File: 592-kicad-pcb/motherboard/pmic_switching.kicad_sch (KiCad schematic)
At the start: 10 parts

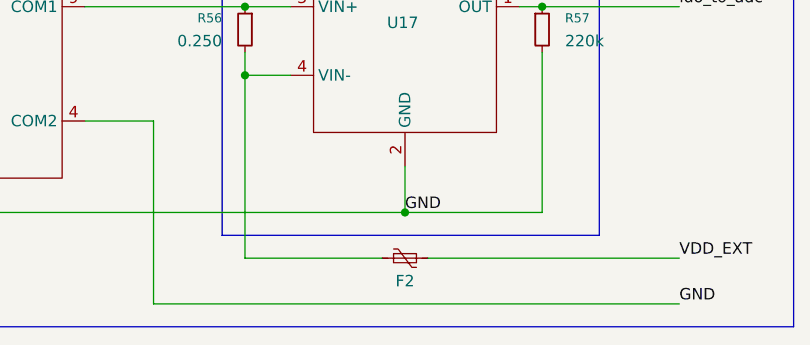
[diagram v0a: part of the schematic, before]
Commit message: fuse, fb info in values
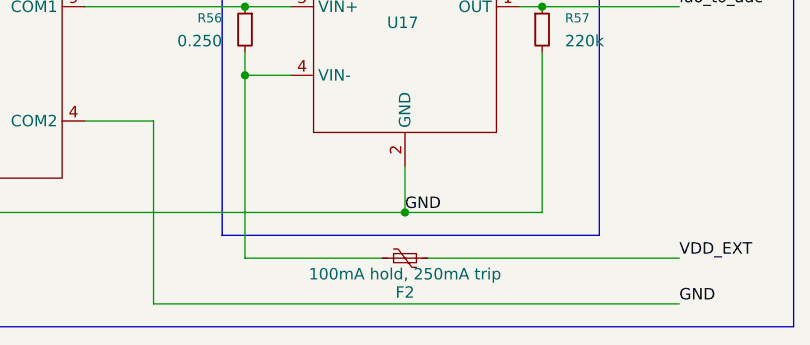
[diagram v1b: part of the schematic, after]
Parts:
- F2: value ~ -> 100mA hold, 250mA trip
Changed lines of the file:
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@@
 		(dnp no)
 		(property "Reference" "F2"
-			(at 137.16 160.02 90)
+			(at 137.16 161.29 90)
 			(effects
 				(font
@@
 			)
 		)
-		(property "Value" "~"
+		(property "Value" "100mA hold, 250mA trip"
 			(at 137.16 159.258 90)
 			(effects

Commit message: updates to routing
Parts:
- renumbered R54 to R60, R56 to R61, R55 to R62, R57 to R63, U20 to U24, U18 to U25, U19 to U26, U16 to U27, U17 to U28
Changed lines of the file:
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@@
 		(on_board yes)
 		(dnp no)
-		(property "Reference" "R57"
+		(property "Reference" "R63"
 			(at 154.94 130.8099 0)
 			(effects
@@
 			(project "motherboard"
 				(path "/5b0c97ac-fa03-4db8-b41b-0eee32b6f55d/f049e4ad-bebe-4338-850a-2727de737ae9/260af3dc-9286-4c76-9c6c-eeb806d3e6e5"
-					(reference "R57")
+					(reference "R63")
 					(unit 1)
 				)
@@
 		(on_board yes)
 		(dnp no)
-		(property "Reference" "U17"
+		(property "Reference" "U28"
 			(at 136.906 131.318 0)
 			(effects
@@
 			(project ""
 				(path "/5b0c97ac-fa03-4db8-b41b-0eee32b6f55d/f049e4ad-bebe-4338-850a-2727de737ae9/260af3dc-9286-4c76-9c6c-eeb806d3e6e5"
-					(reference "U17")
+					(reference "U28")
 					(unit 1)
 				)
@@
 		(on_board yes)
 		(dnp no)
-		(property "Reference" "U20"
+		(property "Reference" "U24"
 			(at 85.344 34.798 0)
 			(effects
@@
 			(project "motherboard"
 				(path "/5b0c97ac-fa03-4db8-b41b-0eee32b6f55d/f049e4ad-bebe-4338-850a-2727de737ae9/260af3dc-9286-4c76-9c6c-eeb806d3e6e5"
-					(reference "U20")
+					(reference "U24")
 					(unit 1)
 				)
@@
 		(on_board yes)
 		(dnp no)
-		(property "Reference" "U19"
+		(property "Reference" "U26"
 			(at 84.836 134.366 0)
 			(effects
@@
 			(project ""
 				(path "/5b0c97ac-fa03-4db8-b41b-0eee32b6f55d/f049e4ad-bebe-4338-850a-2727de737ae9/260af3dc-9286-4c76-9c6c-eeb806d3e6e5"
-					(reference "U19")
+					(reference "U26")
 					(unit 1)
 				)
@@
 		(on_board yes)
 		(dnp no)
-		(property "Reference" "U18"
+		(property "Reference" "U25"
 			(at 85.344 80.518 0)
 			(effects
@@
 			(project ""
 				(path "/5b0c97ac-fa03-4db8-b41b-0eee32b6f55d/f049e4ad-bebe-4338-850a-2727de737ae9/260af3dc-9286-4c76-9c6c-eeb806d3e6e5"
-					(reference "U18")
+					(reference "U25")
 					(unit 1)
 				)
@@
 		(on_board yes)
 		(dnp no)
-		(property "Reference" "U16"
+		(property "Reference" "U27"
 			(at 137.668 78.232 0)
 			(effects
@@
 			(project ""
 				(path "/5b0c97ac-fa03-4db8-b41b-0eee32b6f55d/f049e4ad-bebe-4338-850a-2727de737ae9/260af3dc-9286-4c76-9c6c-eeb806d3e6e5"
-					(reference "U16")
+					(reference "U27")
 					(unit 1)
 				)
@@
 		(on_board yes)
 		(dnp no)
-		(property "Reference" "R55"
+		(property "Reference" "R62"
 			(at 154.94 77.4699 0)
 			(effects
@@
 			(project "motherboard"
 				(path "/5b0c97ac-fa03-4db8-b41b-0eee32b6f55d/f049e4ad-bebe-4338-850a-2727de737ae9/260af3dc-9286-4c76-9c6c-eeb806d3e6e5"
-					(reference "R55")
+					(reference "R62")
 					(unit 1)
 				)
@@
 		(on_board yes)
 		(dnp no)
-		(property "Reference" "R56"
+		(property "Reference" "R61"
 			(at 116.84 130.8099 0)
 			(effects
@@
 			(project "motherboard"
 				(path "/5b0c97ac-fa03-4db8-b41b-0eee32b6f55d/f049e4ad-bebe-4338-850a-2727de737ae9/260af3dc-9286-4c76-9c6c-eeb806d3e6e5"
-					(reference "R56")
+					(reference "R61")
 					(unit 1)
 				)
@@
 		(on_board yes)
 		(dnp no)
-		(property "Reference" "R54"
+		(property "Reference" "R60"
 			(at 116.84 77.4699 0)
 			(effects
@@
 			(project ""
 				(path "/5b0c97ac-fa03-4db8-b41b-0eee32b6f55d/f049e4ad-bebe-4338-850a-2727de737ae9/260af3dc-9286-4c76-9c6c-eeb806d3e6e5"
-					(reference "R54")
-					(unit 1)
-				)
+					(reference "R60")
+					(unit 1)
+				)

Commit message: pins out progress
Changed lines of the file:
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@@
 		(exclude_from_sim no)
 		(at 116.84 63.5 0)
-		(size 41.91 38.1)
+		(size 43.18 38.1)
 		(margins 0.9525 0.9525 0.9525 0.9525)
 		(stroke
@@
 		(exclude_from_sim no)
 		(at 116.84 116.84 0)
-		(size 41.91 38.1)
+		(size 43.18 38.1)
 		(margins 0.9525 0.9525 0.9525 0.9525)
 		(stroke

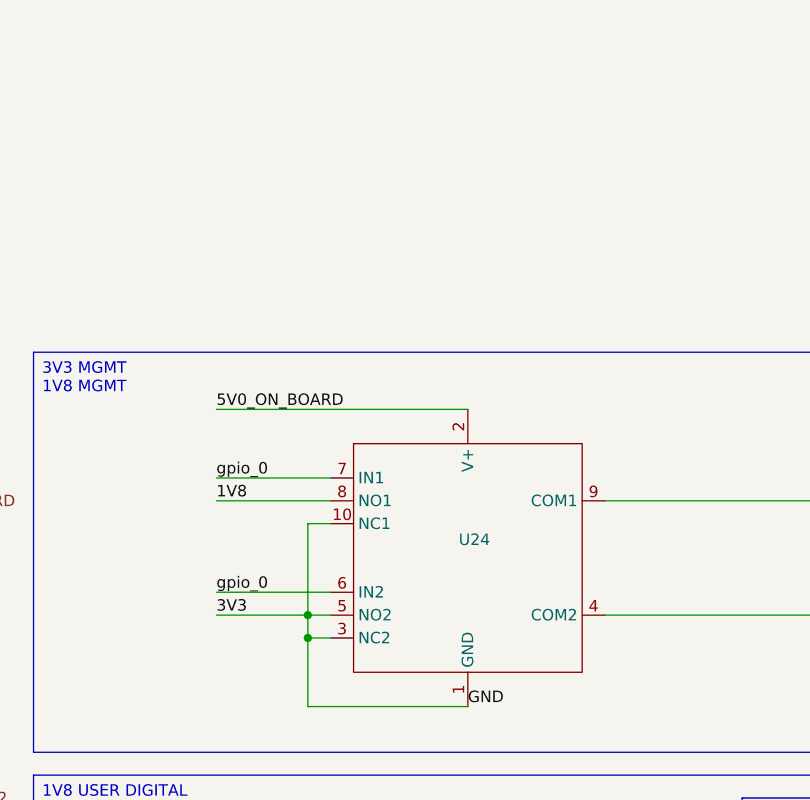
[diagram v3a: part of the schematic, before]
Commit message: can't work on one machine
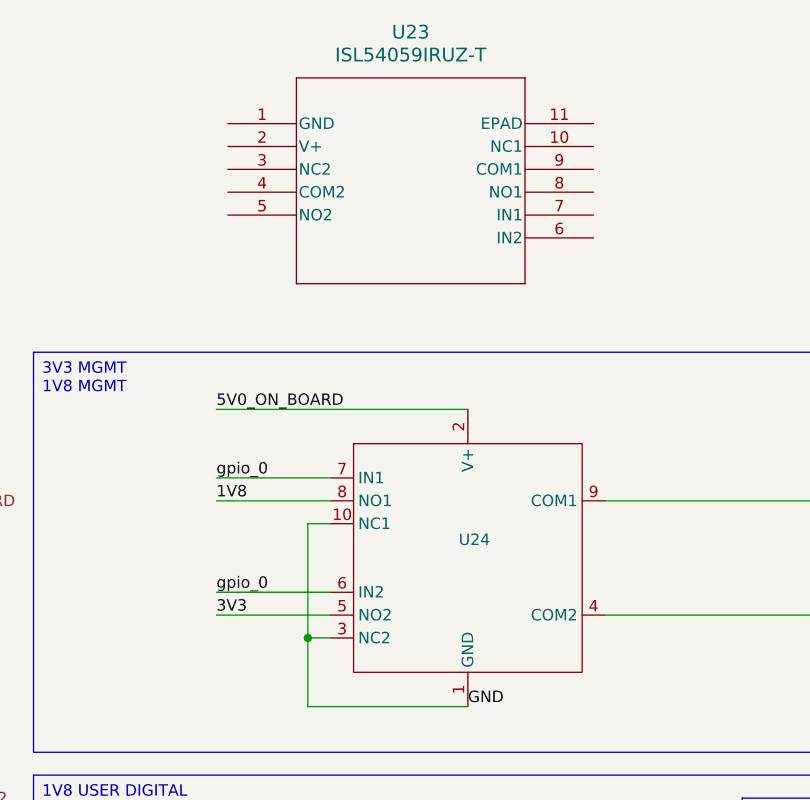
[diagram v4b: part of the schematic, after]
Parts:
- added U23: ISL54059IRUZ-T, UTQFN10_1P85X1P45_INR, symbol 592-partslib:ISL54059IRUZ-T
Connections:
- net 3V3: no longer R62.2, R63.2, U24.1 (GND), U24.10 (NC1), U24.3 (NC2), U25.1 (GND), U25.10 (NC1), U25.3 (NC2), U26.1 (GND), U26.10 (NC1), U26.3 (NC2), U26.4 (COM2), U27.2 (GND), U28.2 (GND)
- new net GND: R62.2, R63.2, U24.1 (GND), U24.10 (NC1), U24.3 (NC2), U25.1 (GND), U25.10 (NC1), U25.3 (NC2), U26.1 (GND), U26.10 (NC1), U26.3 (NC2), U26.4 (COM2), U27.2 (GND), U28.2 (GND)
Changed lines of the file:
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@@
-	)
-	(junction
-		(at 68.58 43.18)
-		(diameter 0)
-		(color 0 0 0 0)
 	)
 	(junction
@@
 	(wire
 		(pts
-			(xy 68.58 43.18) (xy 68.58 33.02)
+			(xy 68.58 33.02) (xy 68.58 45.72)
 		)
 		(stroke
@@
 	(wire
 		(pts
-			(xy 68.58 43.18) (xy 71.12 43.18)
-		)
-		(stroke
-			(width 0)
-			(type default)
-		)
-	)
-	(wire
-		(pts
 			(xy 152.4 76.2) (xy 165.1 76.2)
 		)
@@
 	(wire
 		(pts
-			(xy 68.58 45.72) (xy 68.58 43.18)
-		)
-		(stroke
-			(width 0)
-			(type default)
-		)
-	)
-	(wire
-		(pts
 			(xy 68.58 144.78) (xy 68.58 152.4)
 		)
@@
 	(wire
 		(pts
-			(xy 58.42 43.18) (xy 68.58 43.18)
+			(xy 58.42 43.18) (xy 71.12 43.18)
 		)
 		(stroke
@@
 					(unit 1)
 				)
+			)
+		)
+	)
+	(symbol
+		(lib_id "592-partslib:ISL54059IRUZ-T")
+		(at 59.69 -11.43 0)
+		(unit 1)
+		(exclude_from_sim no)
+		(in_bom yes)
+		(on_board yes)
+		(dnp no)
+		(fields_autoplaced yes)
+		(property "Reference" "U23"
+			(at 80.01 -21.59 0)
+			(effects
+				(font
+					(size 1.524 1.524)
+				)
+			)
+		)
+		(property "Value" "ISL54059IRUZ-T"
+			(at 80.01 -19.05 0)
+			(effects
+				(font
+					(size 1.524 1.524)
+				)
+			)
+		)
+		(property "Footprint" "UTQFN10_1P85X1P45_INR"
+			(at 59.69 -11.43 0)
+			(effects
+				(font
+					(size 1.27 1.27)
+					(italic yes)
+				)
+				(hide yes)
+			)
+		)
+		(property "Datasheet" "ISL54059IRUZ-T"
+			(at 59.69 -11.43 0)
+			(effects
+				(font
+					(size 1.27 1.27)
+					(italic yes)
+				)
+				(hide yes)
+			)
+		)
+		(property "Description" ""
+			(at 59.69 -11.43 0)
+			(effects
+				(font
+					(size 1.27 1.27)
+				)
+				(hide yes)
+			)
+		)
+		(pin "2"
+		)
+		(pin "5"
+		)
+		(pin "9"
+		)
+		(pin "6"
+		)
+		(pin "4"
+		)
+		(pin "3"
+		)
+		(pin "1"
+		)
+		(pin "11"
+		)
+		(pin "10"
+		)
+		(pin "8"
+		)
+		(pin "7"
+		)
+		(instances
+			(project ""
+				(path "/5b0c97ac-fa03-4db8-b41b-0eee32b6f55d/f049e4ad-bebe-4338-850a-2727de737ae9/260af3dc-9286-4c76-9c6c-eeb806d3e6e5"
+					(reference "U23")
+					(unit 1)
+				)

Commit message: check in
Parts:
- removed R61: 0.250, symbol Device:R_Small
- removed R63: 220k, symbol Device:R_Small
- removed U24, U25, U26: ~, uTQFN, symbol 592-partslib:ISL54059IRUZ-T_uTQFN
- removed U28: ~, symbol 592-partslib:INA138NA/3K
- added R16: 0.250, symbol Device:R_Small
- added R17: 220k, symbol Device:R_Small
- added U25, U36: ISL54059IRUZ-T, UTQFN10_1P85X1P45_INR, symbol 592-partslib:ISL54059IRUZ-T
- added U26: INA138NA/3K, Package_TO_SOT_SMD:SOT-23-5_HandSoldering, symbol 592-partslib:INA138NA/3K
- U23: LCSC (none) -> C2673589
- U27: value ~ -> INA138NA/3K; footprint (none) -> Package_TO_SOT_SMD:SOT-23-5_HandSoldering; LCSC (none) -> C47914
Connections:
- net 1V8: now also U23.8 (NO1), U36.8 (NO1)
- net 2V5: now also U25.8 (NO1)
- net 3V3: now also U23.5 (NO2), U36.5 (NO2)
- net 5V0_ON_BOARD: now also U23.2 (V+), U25.2 (V+), U26.5 (V+), U36.2 (V+)
- net AVAIL: now also U25.5 (NO2)
- net GND: now also R17.2, U25.1 (GND), U25.10 (NC1), U25.11 (EPAD), U25.3 (NC2), U25.4 (COM2), U26.2 (GND), U36.1 (GND), U36.10 (NC1), U36.11 (EPAD), U36.3 (NC2)
- net VCCD: now also U23.9 (COM1)
- net VDDA, VDDIO: now also U23.4 (COM2)
- net VDDA1, VDDA2: now also U36.4 (COM2)
- net gpio_0: now also U23.6 (IN2), U23.7 (IN1)
- net gpio_1: now also U36.6 (IN2), U36.7 (IN1)
- net gpio_2: now also U25.7 (IN1)
- net gpio_3: now also U25.6 (IN2)
- net ldo_to_adc: now also R17.1, U26.1 (OUT)
- net at F2.1: now also R16.2, U26.4 (VIN-)
- net at R60.1, U27.3 (VIN+): now also U36.9 (COM1)
- net at U23.1 (GND): now also U23.10 (NC1), U23.11 (EPAD), U23.3 (NC2)
- new net: R16.1, U25.9 (COM1), U26.3 (VIN+)
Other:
- moved on the sheet: F2, R60, R62, U23, U27
